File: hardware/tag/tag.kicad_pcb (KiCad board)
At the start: 2 copper layers, 98.2 x 48.3 mm, 16 parts

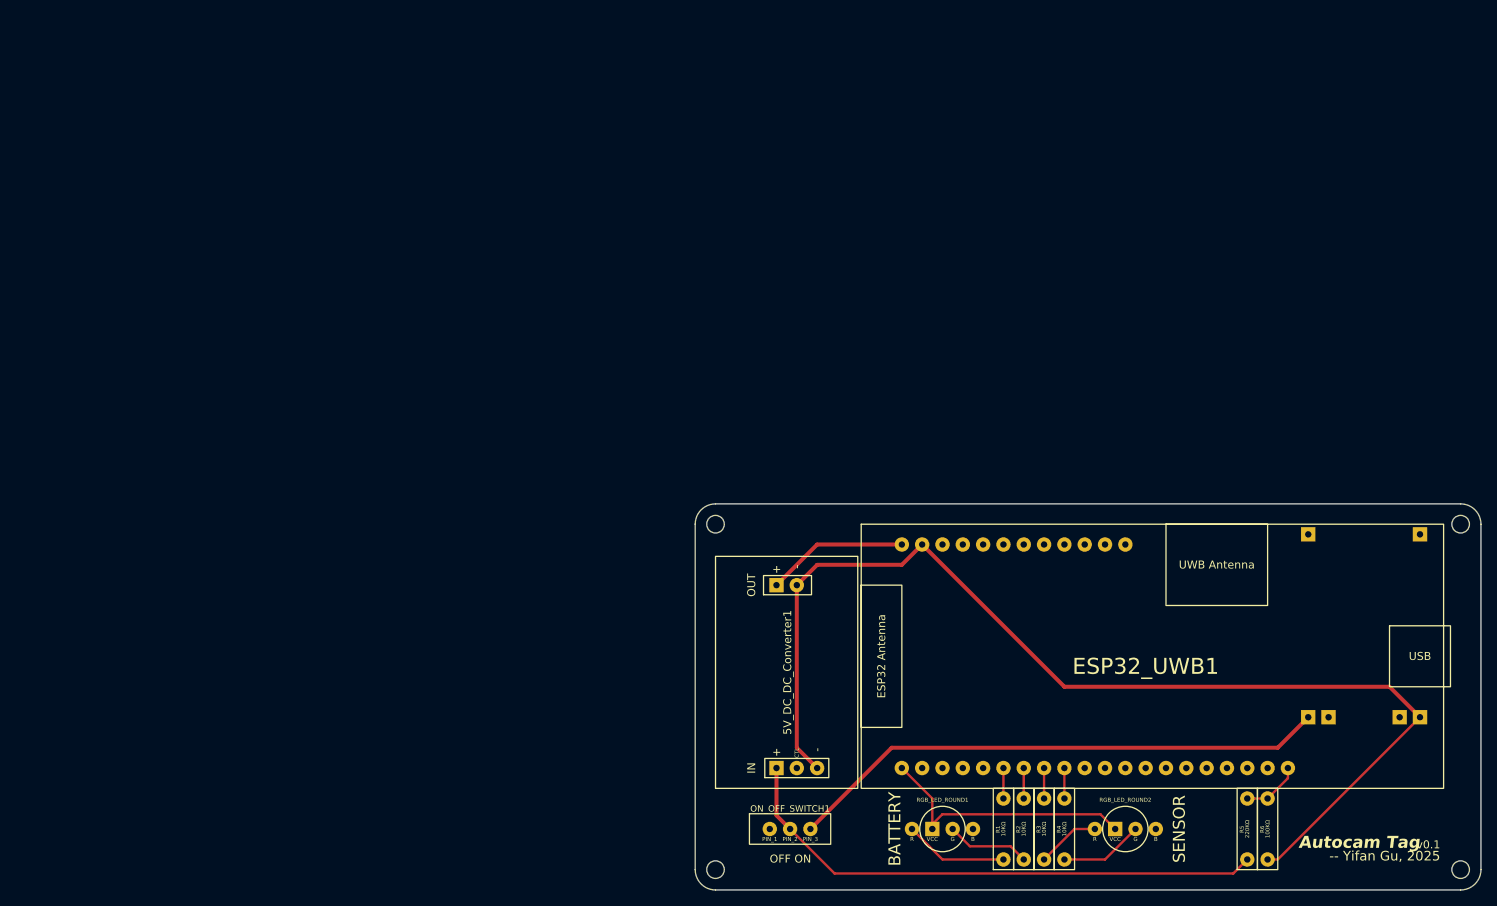
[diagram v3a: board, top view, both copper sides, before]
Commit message: hardware: Move the PCB to near the coordinate origin.
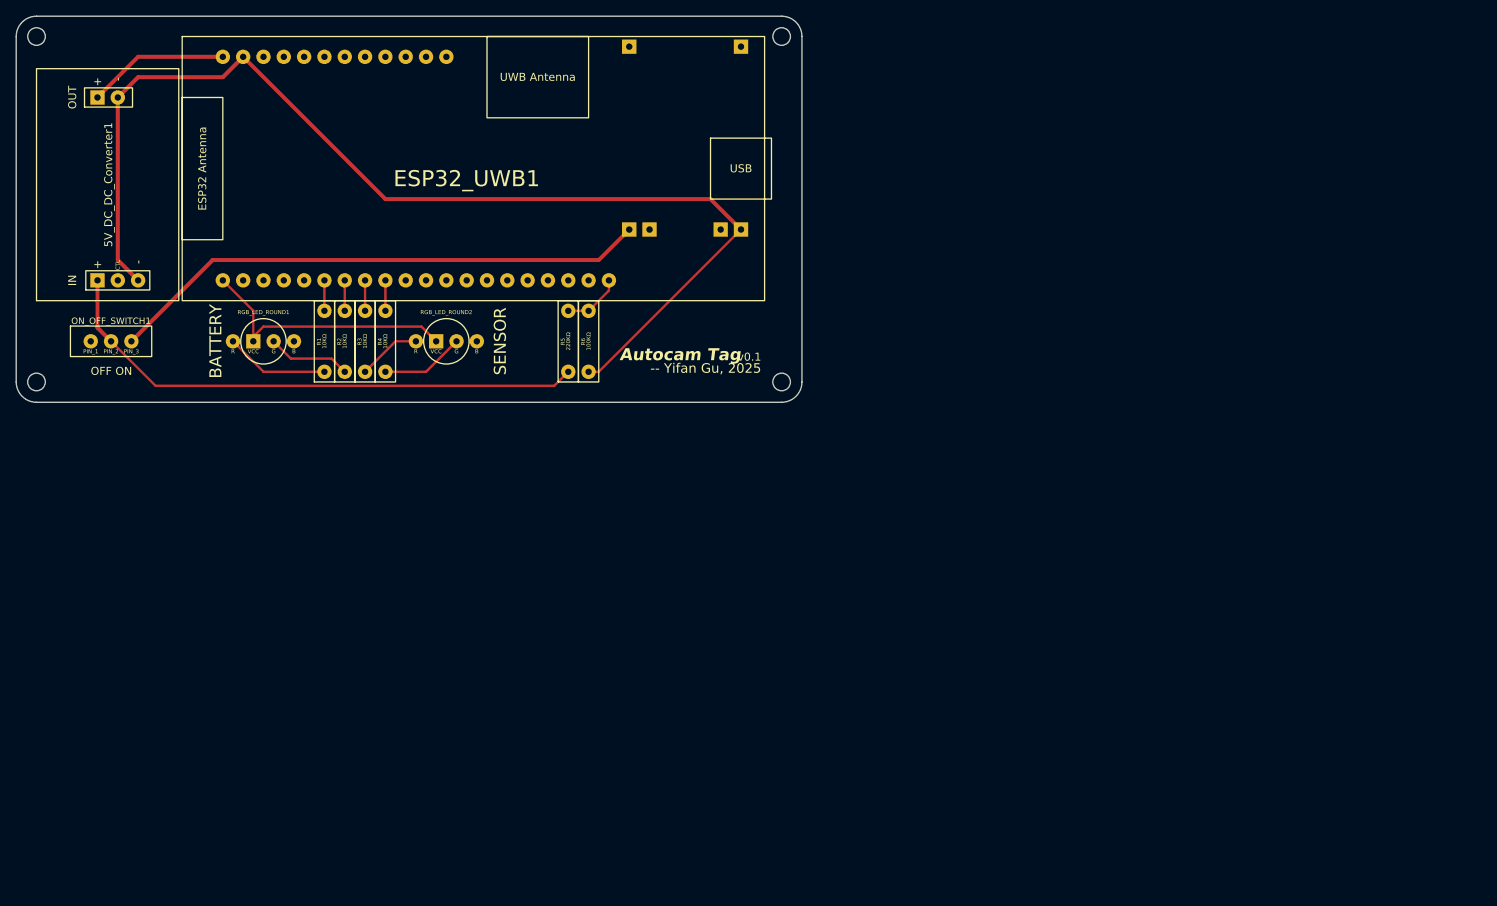
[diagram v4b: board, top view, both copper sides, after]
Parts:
- moved R4 104.5 mm to (61.2, 59.7)
- moved REF** 104.5 mm to (110.7, 61.0)
- moved REF** 104.5 mm to (110.7, 17.8)
- moved 5V_DC_DC_Converter1 104.5 mm to (17.6, 50.8)
- moved Battery_Charger1 104.5 mm to (107.3, 17.8)
- moved ESP32_UWB1 104.5 mm to (35.8, 17.8)
- moved ON_OFF_SWITCH1 104.5 mm to (24.3, 55.9)
- moved R1 104.5 mm to (53.6, 59.7)
- moved R2 104.5 mm to (56.1, 59.7)
- moved R3 104.5 mm to (58.6, 59.7)
- moved R5 104.5 mm to (84.0, 59.7)
- moved REF** 104.5 mm to (17.6, 17.8)
- moved REF** 104.5 mm to (17.6, 61.0)
- moved RGB_LED_ROUND1 104.5 mm to (45.9, 55.9)
- moved R6 104.5 mm to (86.6, 59.7)
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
